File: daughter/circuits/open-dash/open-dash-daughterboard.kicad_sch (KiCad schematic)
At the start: 14 parts, among them J1 Conn_01x01_Female, J2 Conn_01x01_Female, J3 Conn_01x01_Female, J4 Conn_01x01_Female, J43 Conn_02x02_Counter_Clockwise, J46 Conn_02x02_Counter_Clockwise, J5 Conn_02x06_Odd_Even, J6 Conn_IDE_40, J7 Conn_IDE_40, J8 Conn_IDE_40, Q40 Q_AO3401A

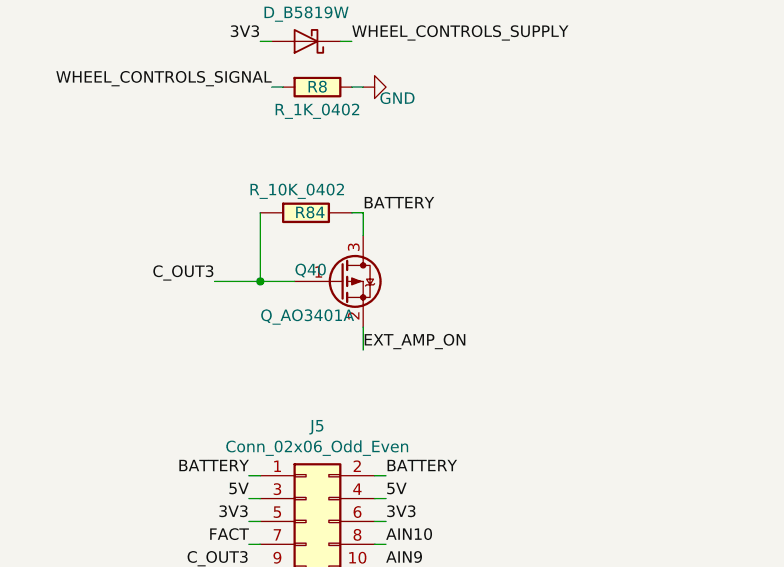
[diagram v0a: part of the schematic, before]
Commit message: Updated hvac circuit
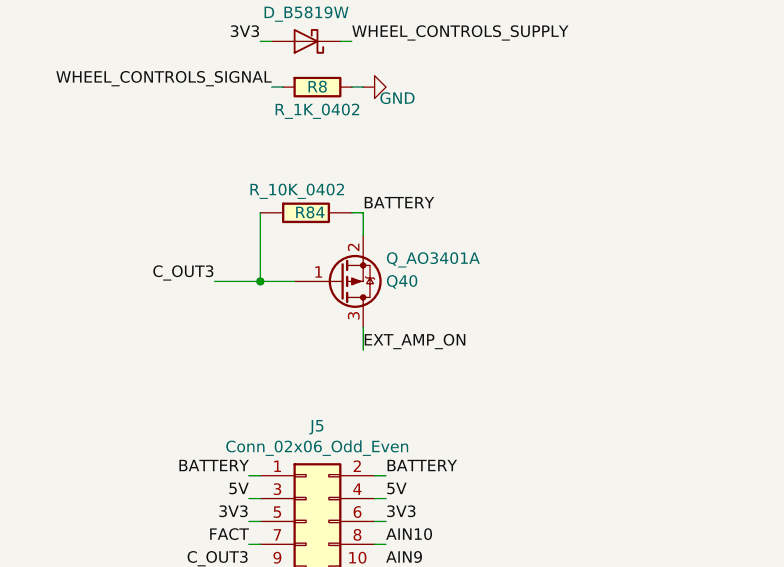
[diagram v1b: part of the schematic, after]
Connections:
- net BATTERY: now also Q40.2 (S); no longer Q40.3 (D)
- net EXT_AMP_ON: now also Q40.3 (D); no longer Q40.2 (S)
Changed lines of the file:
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@@
     (effects (font (size 1.27 1.27)) (justify right bottom))
   )
-  (symbol (lib_id "open-dash-daughterboard-rescue:GND-power") (at 53.34 124.46 90)
+  (symbol (lib_id "open-dash-daughterboard-rescue:GND-power") (at 53.34 124.46 90) (unit 1)
     (in_bom yes) (on_board yes)
     (property "Reference" "#PWR02" (id 0) (at 59.69 124.46 0)
@@
     (pin "1")
   )
-  (symbol (lib_id "open-dash-daughterboard-rescue:GND-power") (at 36.83 124.46 270)
+  (symbol (lib_id "open-dash-daughterboard-rescue:GND-power") (at 36.83 124.46 270) (unit 1)
     (in_bom yes) (on_board yes)
     (property "Reference" "#PWR03" (id 0) (at 30.48 124.46 0)
@@
     (pin "1")
   )
-  (symbol (lib_id "open-dash-daughterboard-rescue:GND-power") (at 46.99 53.34 90)
+  (symbol (lib_id "open-dash-daughterboard-rescue:GND-power") (at 46.99 53.34 90) (unit 1)
     (in_bom yes) (on_board yes)
     (property "Reference" "#PWR04" (id 0) (at 53.34 53.34 0)
@@
     (pin "2")
   )
-  (symbol (lib_id "open-dash-daughterboard-rescue:GND-power") (at 49.53 68.58 90)
+  (symbol (lib_id "open-dash-daughterboard-rescue:GND-power") (at 49.53 68.58 90) (unit 1)
     (in_bom yes) (on_board yes)
     (property "Reference" "#PWR0149" (id 0) (at 55.88 68.58 0)
@@
     (pin "1")
   )
-  (symbol (lib_id "Open_Automation:Q_AO3401A") (at 46.99 90.17 0)
-    (in_bom yes) (on_board yes)
-    (property "Reference" "Q40" (id 0) (at 41.91 88.9 0)
-      (effects (font (size 1.27 1.27)) (justify left))
-    )
-    (property "Value" "Q_AO3401A" (id 1) (at 38.1 93.98 0)
-      (effects (font (size 1.27 1.27)) (justify left))
-    )
-    (property "Footprint" "Package_TO_SOT_SMD:SOT-23" (id 2) (at 52.07 87.63 0)
-      (effects (font (size 1.27 1.27)) hide)
-    )
-    (property "Datasheet" "https://datasheet.lcsc.com/lcsc/1810171817_Alpha-&-Omega-Semicon-AO3401A_C15127.pdf" (id 3) (at 52.07 88.9 0)
-      (effects (font (size 1.27 1.27)) hide)
-    )
-    (property "Part Number" "AO3401A" (id 4) (at 54.61 86.36 0)
+  (symbol (lib_id "Open_Automation:Q_AO3401A") (at 46.99 90.17 0) (mirror x) (unit 1)
+    (in_bom yes) (on_board yes)
+    (property "Reference" "Q40" (id 0) (at 52.07 90.17 0)
+      (effects (font (size 1.27 1.27)) (justify left))
+    )
+    (property "Value" "Q_AO3401A" (id 1) (at 52.07 87.63 0)
+      (effects (font (size 1.27 1.27)) (justify left))
+    )
+    (property "Footprint" "Package_TO_SOT_SMD:SOT-23" (id 2) (at 52.07 92.71 0)
+      (effects (font (size 1.27 1.27)) hide)
+    )
+    (property "Datasheet" "https://datasheet.lcsc.com/lcsc/1810171817_Alpha-&-Omega-Semicon-AO3401A_C15127.pdf" (id 3) (at 52.07 91.44 0)
+      (effects (font (size 1.27 1.27)) hide)
+    )
+    (property "Part Number" "AO3401A" (id 4) (at 54.61 93.98 0)
       (effects (font (size 1.524 1.524)) hide)
     )
-    (property "LCSC" "C15127" (id 5) (at 54.61 83.82 0)
+    (property "LCSC" "C15127" (id 5) (at 54.61 96.52 0)
       (effects (font (size 1.27 1.27)) hide)
     )
@@
     (pin "3")
   )
-  (symbol (lib_id "Open_Automation:R_10K_0402") (at 43.18 82.55 270)
+  (symbol (lib_id "Open_Automation:R_10K_0402") (at 43.18 82.55 270) (unit 1)
     (in_bom yes) (on_board yes)
     (property "Reference" "R84" (id 0) (at 41.91 82.55 90)
@@
     (pin "2")
   )
-  (symbol (lib_id "open-dash-daughterboard-rescue:GND-open-automation") (at 167.64 72.39 90)
+  (symbol (lib_id "open-dash-daughterboard-rescue:GND-open-automation") (at 167.64 72.39 90) (unit 1)
     (in_bom yes) (on_board yes)
     (property "Reference" "#PWR0158" (id 0) (at 173.99 72.39 0)
@@
     (pin "2")
   )
-  (symbol (lib_id "open-dash-daughterboard-rescue:Conn_02x02_Counter_Clockwise-Connector_Generic") (at 43.18 135.89 0)
+  (symbol (lib_id "open-dash-daughterboard-rescue:Conn_02x02_Counter_Clockwise-Connector_Generic") (at 43.18 135.89 0) (unit 1)
     (in_bom yes) (on_board yes)
     (property "Reference" "J43" (id 0) (at 44.45 130.3782 0))
@@
     (pin "4")
   )
-  (symbol (lib_id "open-dash-daughterboard-rescue:GND-power") (at 36.83 135.89 270)
+  (symbol (lib_id "open-dash-daughterboard-rescue:GND-power") (at 36.83 135.89 270) (unit 1)
     (in_bom yes) (on_board yes)
     (property "Reference" "#PWR0159" (id 0) (at 30.48 135.89 0)
@@
     (pin "9")
   )
-  (symbol (lib_id "open-dash-daughterboard-rescue:Conn_02x02_Counter_Clockwise-Connector_Generic") (at 43.18 148.59 0)
+  (symbol (lib_id "open-dash-daughterboard-rescue:Conn_02x02_Counter_Clockwise-Connector_Generic") (at 43.18 148.59 0) (unit 1)
     (in_bom yes) (on_board yes)
     (property "Reference" "J46" (id 0) (at 44.45 143.0782 0))
@@
     (pin "4")
   )
-  (symbol (lib_id "open-dash-daughterboard-rescue:GND-power") (at 36.83 148.59 270)
+  (symbol (lib_id "open-dash-daughterboard-rescue:GND-power") (at 36.83 148.59 270) (unit 1)
     (in_bom yes) (on_board yes)
     (property "Reference" "#PWR0177" (id 0) (at 30.48 148.59 0)
@@
     (pin "1")
   )
-  (symbol (lib_id "power:GND") (at 27.94 36.83 0)
+  (symbol (lib_id "power:GND") (at 27.94 36.83 0) (unit 1)
     (in_bom yes) (on_board yes)
     (property "Reference" "#PWR01" (id 0) (at 27.94 43.18 0)
@@
     (pin "1")
   )
-  (symbol (lib_id "open-dash-daughterboard-rescue:GND-power") (at 228.6 86.36 0)
+  (symbol (lib_id "open-dash-daughterboard-rescue:GND-power") (at 228.6 86.36 0) (unit 1)
     (in_bom yes) (on_board yes)
     (property "Reference" "#PWR014" (id 0) (at 228.6 92.71 0)
@@
     (pin "1")
   )
-  (symbol (lib_id "open-dash-daughterboard-rescue:GND-power") (at 281.94 86.36 0)
+  (symbol (lib_id "open-dash-daughterboard-rescue:GND-power") (at 281.94 86.36 0) (unit 1)
     (in_bom yes) (on_board yes)
     (property "Reference" "#PWR019" (id 0) (at 281.94 92.71 0)
@@
     (pin "1")
   )
-  (symbol (lib_id "open-dash-daughterboard-rescue:GND-power") (at 294.64 86.36 0)
+  (symbol (lib_id "open-dash-daughterboard-rescue:GND-power") (at 294.64 86.36 0) (unit 1)
     (in_bom yes) (on_board yes)
     (property "Reference" "#PWR024" (id 0) (at 294.64 92.71 0)
@@
     (pin "1")
   )
-  (symbol (lib_id "open-dash-daughterboard-rescue:GND-open-automation") (at 153.67 86.36 0)
+  (symbol (lib_id "open-dash-daughterboard-rescue:GND-open-automation") (at 153.67 86.36 0) (unit 1)
     (in_bom yes) (on_board yes)
     (property "Reference" "#PWR07" (id 0) (at 153.67 92.71 0)
@@
     (pin "1")
   )
-  (symbol (lib_id "open-dash-daughterboard-rescue:GND-open-automation") (at 166.37 86.36 0)
+  (symbol (lib_id "open-dash-daughterboard-rescue:GND-open-automation") (at 166.37 86.36 0) (unit 1)
     (in_bom yes) (on_board yes)
     (property "Reference" "#PWR010" (id 0) (at 166.37 92.71 0)
@@
     (pin "1")
   )
-  (symbol (lib_id "open-dash-daughterboard-rescue:GND-open-automation") (at 215.9 86.36 0)
+  (symbol (lib_id "open-dash-daughterboard-rescue:GND-open-automation") (at 215.9 86.36 0) (unit 1)
     (in_bom yes) (on_board yes)
     (property "Reference" "#PWR012" (id 0) (at 215.9 92.71 0)
@@
     (pin "1")
   )
-  (symbol (lib_id "open-dash-daughterboard-rescue:GND-power") (at 295.91 64.77 90)
+  (symbol (lib_id "open-dash-daughterboard-rescue:GND-power") (at 295.91 64.77 90) (unit 1)
     (in_bom yes) (on_board yes)
     (property "Reference" "#PWR020" (id 0) (at 302.26 64.77 0)
@@
       (reference "D9") (unit 1) (value "D_B5819W") (footprint "Diode_SMD:D_SOD-123")
     )
-    (path "/00000000-0000-0000-0000-00006077d777/00000000-0000-0000-0000-00005cc255be"
-      (reference "D10") (unit 1) (value "LED_G") (footprint "Diode_SMD:D_0603_1608Metric_Pad1.05x0.95mm_HandSolder")
-    )
-    (path "/00000000-0000-0000-0000-00006077d777/00000000-0000-0000-0000-00005cc26acf"
-      (reference "D11") (unit 1) (value "LED_G") (footprint "Diode_SMD:D_0603_1608Metric_Pad1.05x0.95mm_HandSolder")
-    )
-    (path "/00000000-0000-0000-0000-00006077d777/00000000-0000-0000-0000-00005cc27619"
-      (reference "D12") (unit 1) (value "LED_G") (footprint "Diode_SMD:D_0603_1608Metric_Pad1.05x0.95mm_HandSolder")
-    )
     (path "/00000000-0000-0000-0000-000060d3331d/00000000-0000-0000-0000-00005ccc0b80"
       (reference "D13") (unit 1) (value "PESD1CAN-UX") (footprint "Package_TO_SOT_SMD:SOT-23")
     )
+    (path "/00000000-0000-0000-0000-000060ddd162/0649ff2a-0437-40ca-bb4d-ef8d356a0cbb"
+      (reference "D?") (unit 1) (value "D_MURA120") (footprint "Diode_SMD:D_SMA_Handsoldering")
+    )
     (path "/00000000-0000-0000-0000-00006077d777/00000000-0000-0000-0000-00005cc89c1f"
